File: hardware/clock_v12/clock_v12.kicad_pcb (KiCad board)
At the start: 2 copper layers, 119 x 92 mm, 225 parts, among them J1 RJ45, J10 KH-BNC50-3511, J11 KH-BNC50-3511, J12 Conn_01x08_Pin, J13 KH-BNC50-3511, J14 Conn_01x02_Pin, J2 Conn_01x03, J3 KH-BNC50-3511, J4 USB_C_Receptacle, J5 Conn_01x06_Pin, J6 Conn_01x03_Pin, J7 KH-BNC50-3511, J8 Conn_01x02_Pin, J9 KH-BNC50-3511, Q1 2N7002, Q10 2N7002, Q9 2N7002, SW1 SW_Push_4PDT, SW2 SW_SPDT, U1 ADA4807-1, U10 STM32F405RGTx, U11 AMS1117-3.3, U12 BA50DD0WHFP-TR, U13 M24C02-RMN, U14 CH340C, U15 USBLC6-2P6, U16 TLV3603DCKR, U17 SN74LVC1G14DBV, U18 TMP112AIDRLR, U19 SN74LVC1G14DBV, U2 SN74LVC1G14DBV, U20 SN74LVC1G14DBV, U21 SN74LVC1G14DBV, U23 TPS63060, U3 SN74LVC1G14DBV, U4 ADA4807-1, U5 ADA4807-1, U6 TLV3603DCKR, U7 SN74LVC1G14DBV, U8 TLV3603DCKR, U9 L78L05_SOT89, Y1 MultiOsc, Y2 16MHz

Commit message: add 3d model for RJ45 connector
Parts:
- J1: footprint Connector_RJ:RJ45_Amphenol_RJHSE5380 -> blinky_footprints:RJ45_Amphenol_RJHSE5380
- J4: footprint Connector_USB:USB_C_Receptacle_HRO_TYPE-C-31-M-12 -> blinky_footprints:USB_C_Receptacle_HRO_TYPE-C-31-M-12

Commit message: update clock_v12 to kicad 8
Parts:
- D4: footprint Diode_SMD:D_SOD-523 -> Diode_SMD:D_SOD-123
- J4: footprint blinky_footprints:USB_C_Receptacle_HRO_TYPE-C-31-M-12 -> Connector_USB:USB_C_Receptacle_HRO_TYPE-C-31-M-12
- U23: footprint blinky_footprints:Texas_S-PWSON-N10_ThermalVias-CJ -> Package_SON:Texas_S-PWSON-N10_ThermalVias
- moved D4 1.10 mm to (113.4, 69.0)
- moved U15 0.12 mm to (107.7, 87.9)
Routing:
- net unconnected-(J4-SHIELD-PadS1)_0: track 17.0 -> 0.00 mm
- net GND: track 1581.7 -> 1582.4 mm

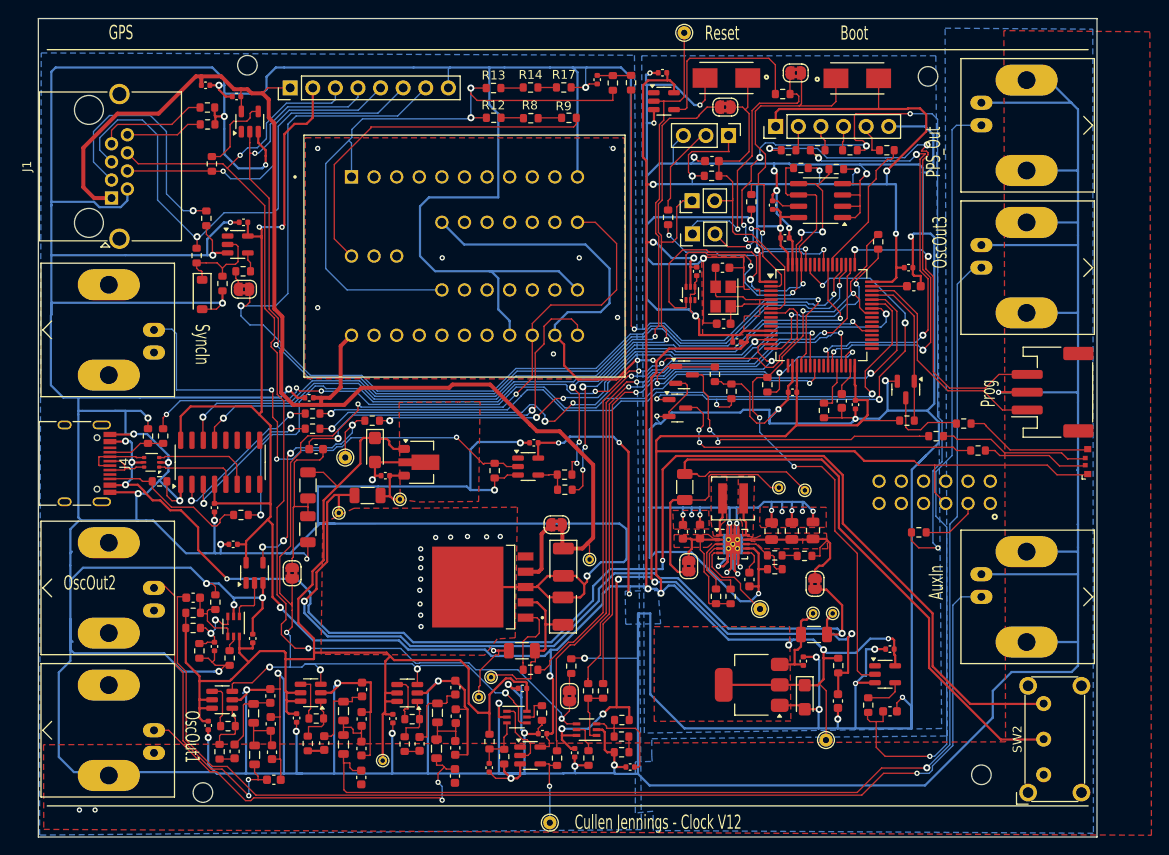
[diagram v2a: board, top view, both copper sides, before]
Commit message: update on clock for kicad 8
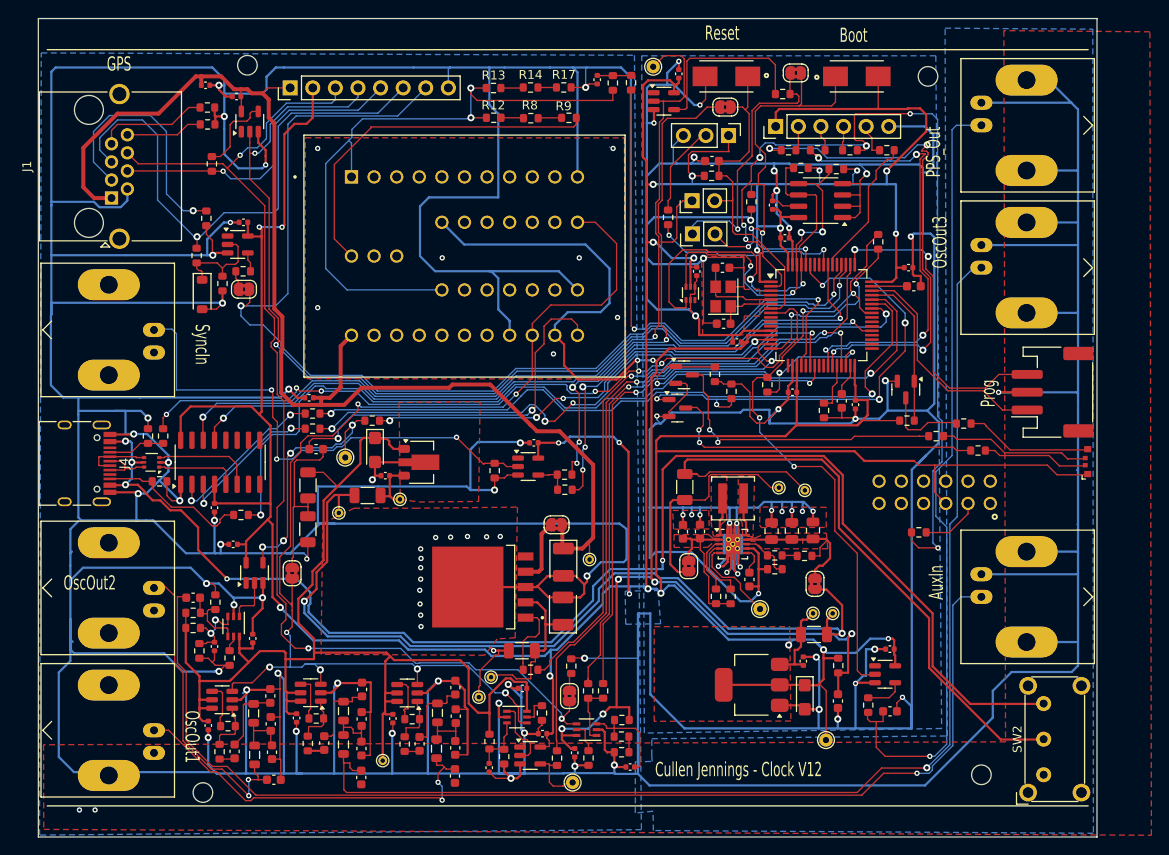
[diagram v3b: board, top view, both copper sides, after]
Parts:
- moved TP10 5.19 mm to (155.1, 123.9)
- moved TP8 5.17 mm to (164.1, 43.4)
- moved C58 1.84 mm to (167.0, 44.2), turned to 90 degrees
- moved S3 0.23 mm to (187.0, 44.5)
- moved S1 0.18 mm to (172.3, 44.5)
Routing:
- net Net-(R57-Pad2): track 8.52 -> 6.92 mm, vias 1 -> 0
- net GND: track 1582.4 -> 1583.8 mm
- net /USB_RTS: track 96.6 -> 97.8 mm
- net +3.3V: track 548.7 -> 549.3 mm

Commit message: move USB on clock v12
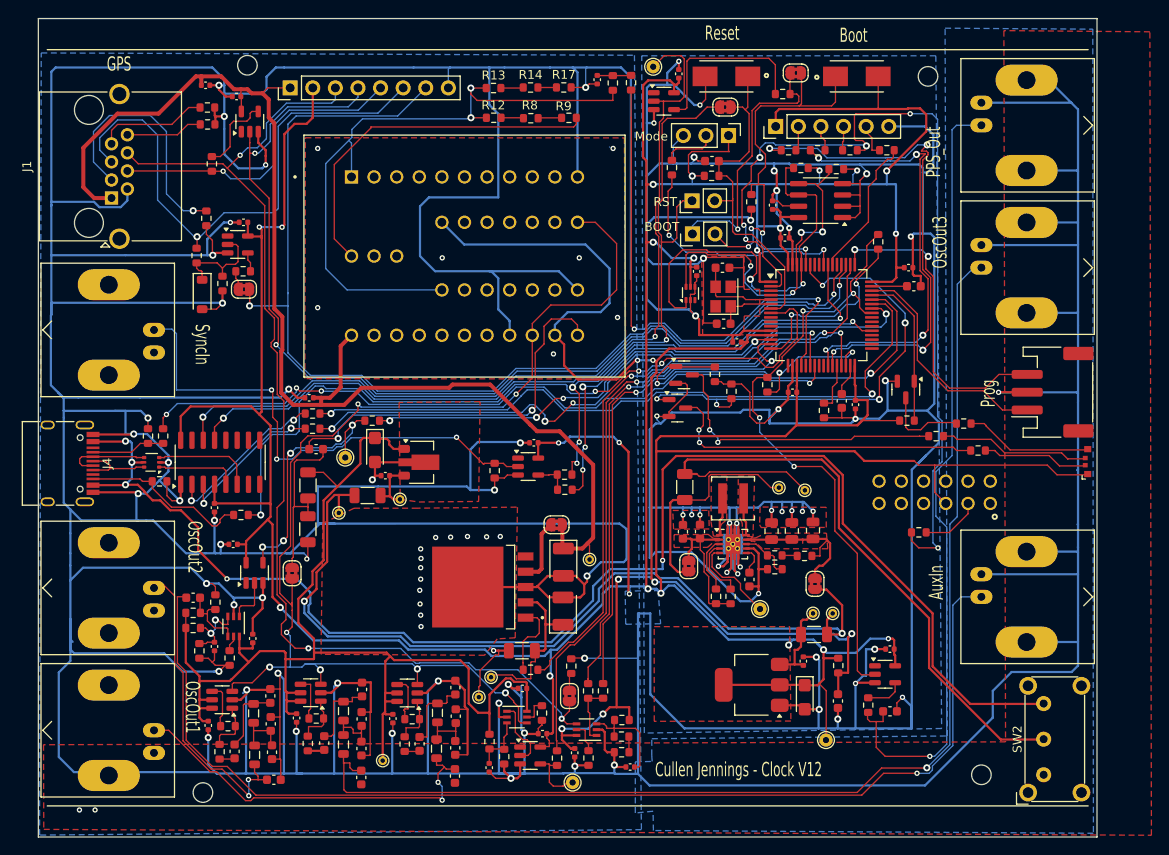
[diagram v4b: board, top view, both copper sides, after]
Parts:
- moved R80 5.60 mm to (166.2, 54.8)
- moved J4 1.90 mm to (97.1, 88.0)
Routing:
- net GND: track 1583.8 -> 1591.6 mm
- net /LED3: track 21.8 -> 27.5 mm
- net VBUS: track 158.8 -> 162.8 mm
- net Net-(J6-Pin_2): track 9.94 -> 6.10 mm
- net /GPS_TX1: track 126.4 -> 122.7 mm
- net Net-(J4-D+-PadA6): track 6.34 -> 8.54 mm
- net Net-(J4-D--PadA7): track 7.33 -> 9.41 mm
- net Net-(J4-CC2): track 17.2 -> 19.2 mm
- net Net-(J4-CC1): track 6.39 -> 8.39 mm
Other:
- board text added: "BOOT"
- board text added: "Mode"
- board text added: "RST"

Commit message: clean up 3d models for clock
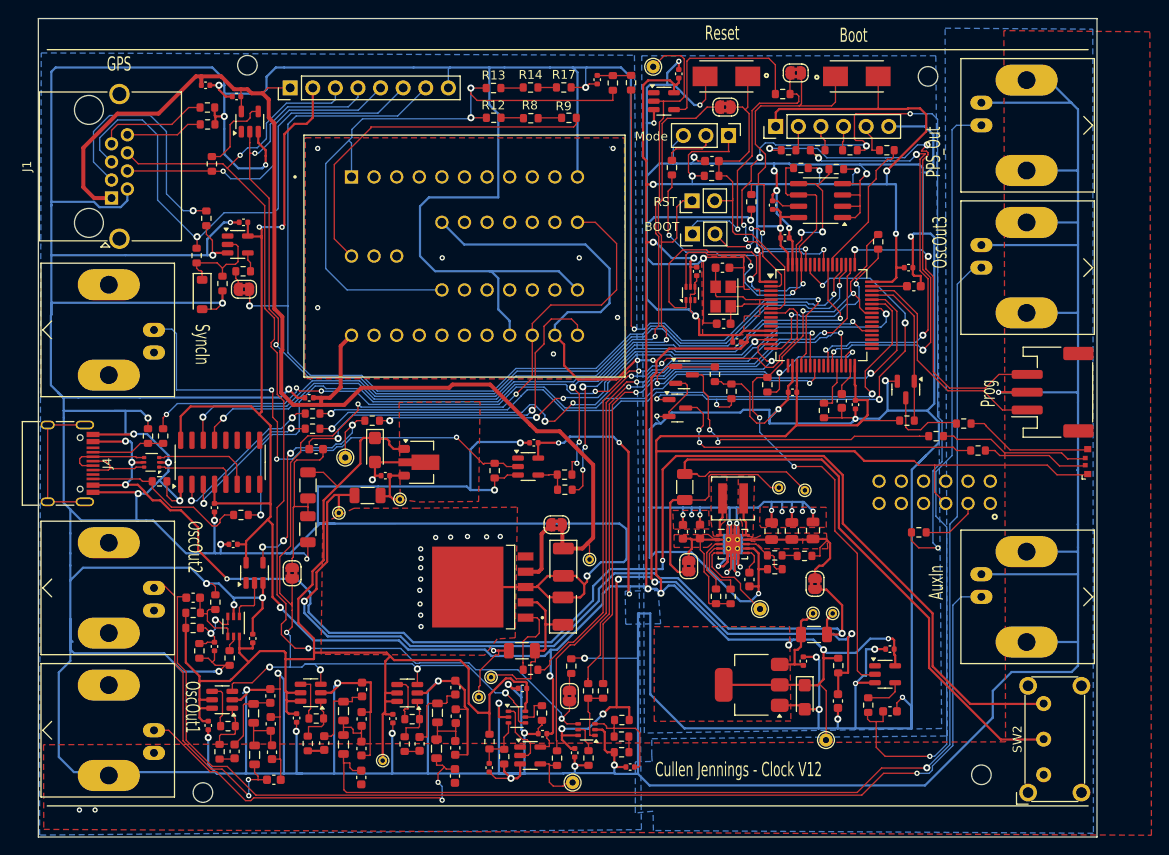
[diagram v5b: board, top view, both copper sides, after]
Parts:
- J4: footprint Connector_USB:USB_C_Receptacle_HRO_TYPE-C-31-M-12 -> blinky_footprints:USB_C_Receptacle_HRO_TYPE-C-31-M-12
- U23: footprint Package_SON:Texas_S-PWSON-N10_ThermalVias -> blinky_footprints:Texas_S-PWSON-N10_ThermalVias-CJ
- U6, U8: footprint blinky_footprints:SC70_DCK_TEX -> Package_TO_SOT_SMD:SOT-363_SC-70-6
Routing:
- net unconnected-(J4-SHIELD-PadS1)_1: track 0.00 -> 17.0 mm
